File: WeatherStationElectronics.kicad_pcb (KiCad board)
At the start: 2 copper layers, 99.5 x 86 mm, 8 parts, among them J1 Barrel_Jack, SW1 SW_SPST, U1 ESP32-C3-DevKitM-1, U3 DHT11, U4 BMP280

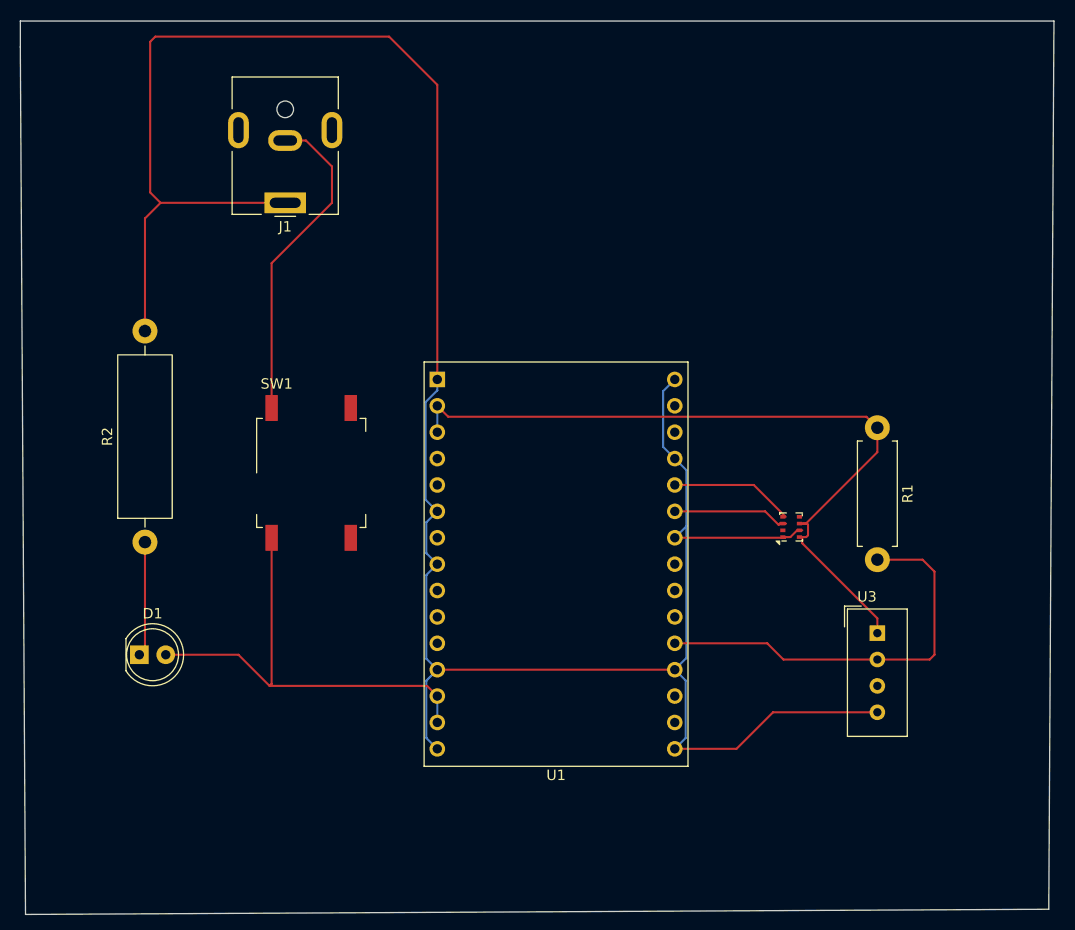
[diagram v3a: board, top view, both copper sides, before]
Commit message: Add mounting holes to the PCB
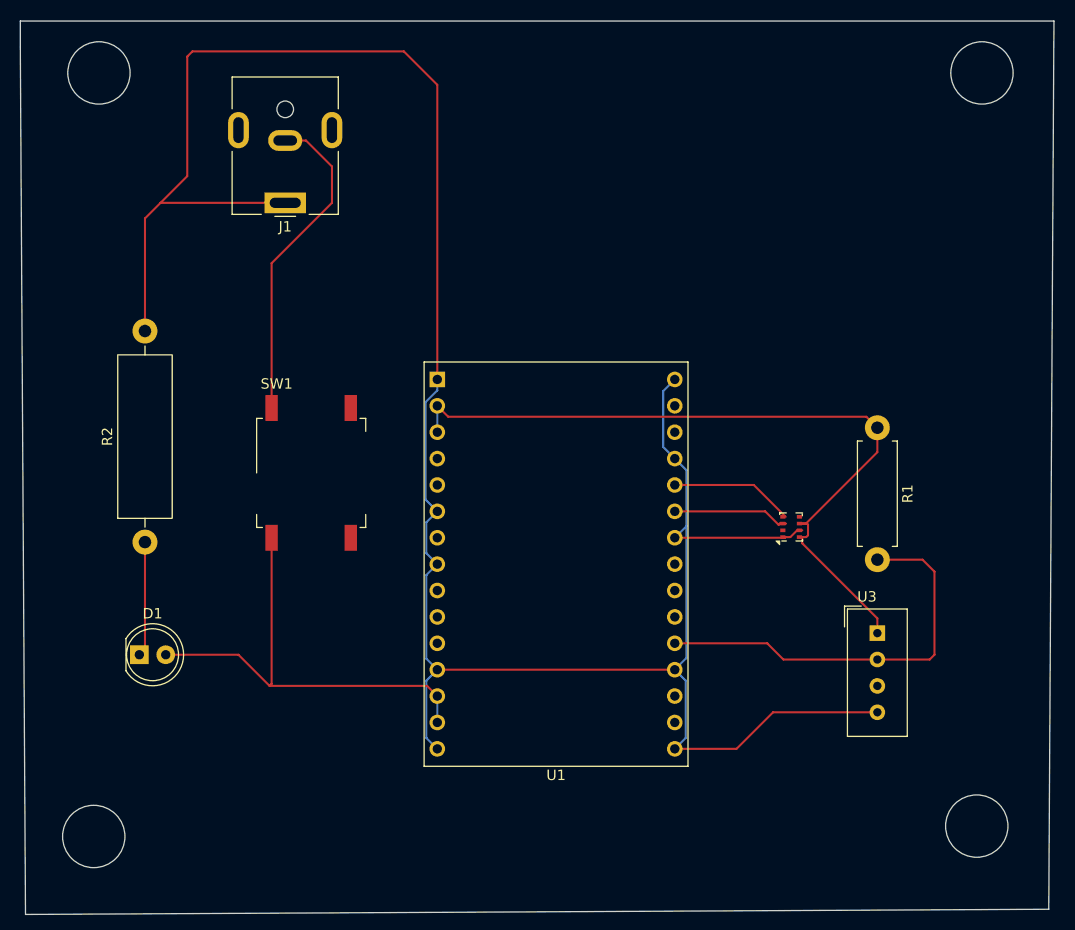
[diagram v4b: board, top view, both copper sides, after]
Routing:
- net GND: track 235.5 -> 230.6 mm
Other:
- outline, holes or cut-outs redrawn
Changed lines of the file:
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@@
 			)
 		)
-		(property "Datasheet" ""
+		(property "Datasheet" "~"
 			(at 0 0 0)
 			(layer "F.Fab")
@@
 			)
 		)
-		(property "Datasheet" ""
+		(property "Datasheet" "~"
 			(at 0 0 0)
 			(unlocked yes)
@@
 			)
 		)
-		(property "Datasheet" ""
+		(property "Datasheet" "~"
 			(at 0 0 90)
 			(layer "F.Fab")
@@
 		)
 		(property "Value" "Barrel_Jack"
-			(at -0.5 14.5 0)
+			(at -0.07 13.505 0)
 			(layer "F.Fab")
 			(effects
@@
 			)
 		)
-		(property "Datasheet" ""
+		(property "Datasheet" "~"
 			(at 0 0 180)
 			(unlocked yes)
@@
 			)
 		)
-		(property "Datasheet" ""
+		(property "Datasheet" "~"
 			(at 0 0 90)
 			(layer "F.Fab")
@@
 		(layer "Edge.Cuts")
 	)
+	(gr_circle
+		(center 48 54)
+		(end 51 54)
+		(stroke
+			(width 0.05)
+			(type solid)
+		)
+		(fill no)
+		(layer "Edge.Cuts")
+	)
 	(gr_line
 		(start 139.93 49.005)
@@
 		(layer "Edge.Cuts")
 	)
+	(gr_circle
+		(center 47.5 127.5)
+		(end 50.5 127.5)
+		(stroke
+			(width 0.05)
+			(type solid)
+		)
+		(fill no)
+		(layer "Edge.Cuts")
+	)
 	(gr_line
 		(start 40.93 135.005)
@@
 		(layer "Edge.Cuts")
 	)
+	(gr_circle
+		(center 132.5 126.5)
+		(end 135.5 126.5)
+		(stroke
+			(width 0.05)
+			(type solid)
+		)
+		(fill no)
+		(layer "Edge.Cuts")
+	)
+	(gr_circle
+		(center 133 54)
+		(end 136 54)
+		(stroke
+			(width 0.05)
+			(type solid)
+		)
+		(fill no)
+		(layer "Edge.Cuts")
+	)
 	(gr_line
 		(start 40.43 49.005)
@@
 	)
 	(segment
+		(start 56.5 52.425)
+		(end 56.5 63.935)
+		(width 0.2)
+		(layer "F.Cu")
+		(net 3)
+	)
+	(segment
 		(start 115.205 98.03)
 		(end 115.705 98.03)
@@
 	)
 	(segment
-		(start 53.43 50.505)
-		(end 52.93 51.005)
-		(width 0.2)
-		(layer "F.Cu")
-		(net 3)
-	)
-	(segment
-		(start 75.93 50.505)
-		(end 53.43 50.505)
-		(width 0.2)
-		(layer "F.Cu")
-		(net 3)
-	)
-	(segment
-		(start 80.57 55.145)
-		(end 75.93 50.505)
-		(width 0.2)
-		(layer "F.Cu")
-		(net 3)
-	)
-	(segment
 		(start 114.105 98.68)
 		(end 114.555 98.68)
@@
 	)
 	(segment
+		(start 77.35 51.925)
+		(end 57 51.925)
+		(width 0.2)
+		(layer "F.Cu")
+		(net 3)
+	)
+	(segment
 		(start 66.93 66.505)
 		(end 65.93 66.505)
@@
 	)
 	(segment
+		(start 80.57 55.145)
+		(end 77.35 51.925)
+		(width 0.2)
+		(layer "F.Cu")
+		(net 3)
+	)
+	(segment
+		(start 109.37 119.065)
+		(end 103.43 119.065)
+		(width 0.2)
+		(layer "F.Cu")
+		(net 3)
+	)
+	(segment
+		(start 52.43 68.005)
+		(end 53.93 66.505)
+		(width 0.2)
+		(layer "F.Cu")
+		(net 3)
+	)
+	(segment
+		(start 57 51.925)
+		(end 56.5 52.425)
+		(width 0.2)
+		(layer "F.Cu")
+		(net 3)
+	)
+	(segment
+		(start 122.93 115.545)
+		(end 112.89 115.545)
+		(width 0.2)
+		(layer "F.Cu")
+		(net 3)
+	)
+	(segment
 		(start 80.57 83.505)
 		(end 80.57 55.145)
@@
 	)
 	(segment
-		(start 109.37 119.065)
-		(end 103.43 119.065)
-		(width 0.2)
-		(layer "F.Cu")
-		(net 3)
-	)
-	(segment
-		(start 52.43 68.005)
-		(end 53.93 66.505)
-		(width 0.2)
-		(layer "F.Cu")
-		(net 3)
-	)
-	(segment
-		(start 122.93 115.545)
-		(end 112.89 115.545)
-		(width 0.2)
-		(layer "F.Cu")
-		(net 3)
-	)
-	(segment
 		(start 80.57 111.445)
 		(end 103.43 111.445)
@@
 	)
 	(segment
-		(start 52.93 51.005)
-		(end 52.93 65.505)
+		(start 56.5 63.935)
+		(end 53.93 66.505)
 		(width 0.2)
 		(layer "F.Cu")
@@
 		(width 0.2)
 		(layer "F.Cu")
-		(net 3)
-	)
-	(segment
-		(start 52.93 65.505)
-		(end 53.93 66.505)
-		(width 0.2)
-		(layer "F.Cu")

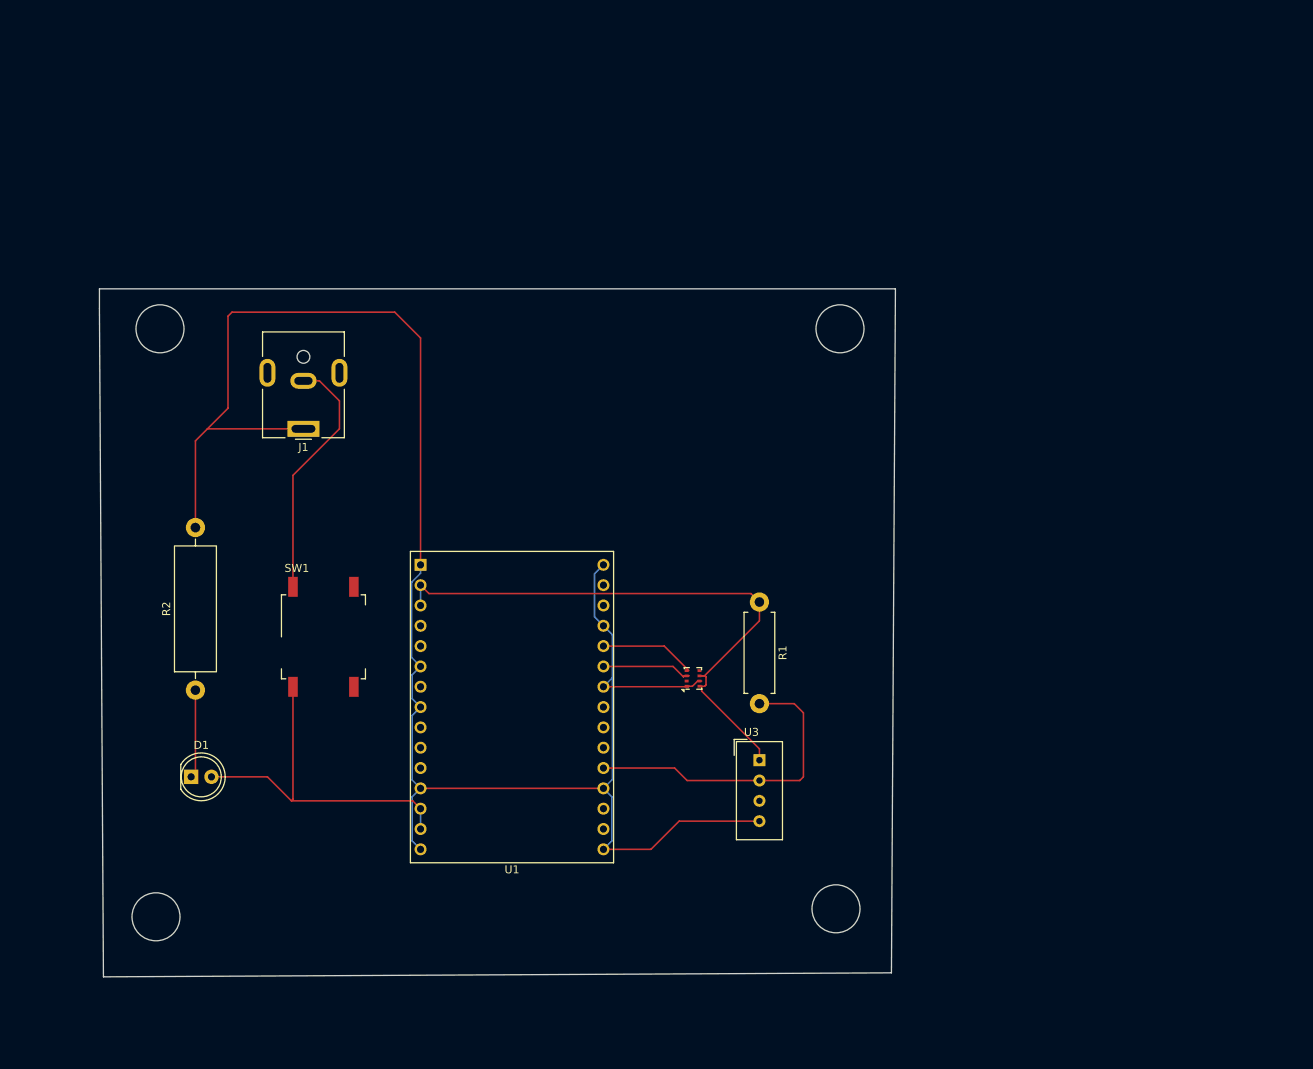
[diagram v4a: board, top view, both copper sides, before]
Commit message: update PCB
Make mounting holes and fill all the board area with copper connected to
the ground
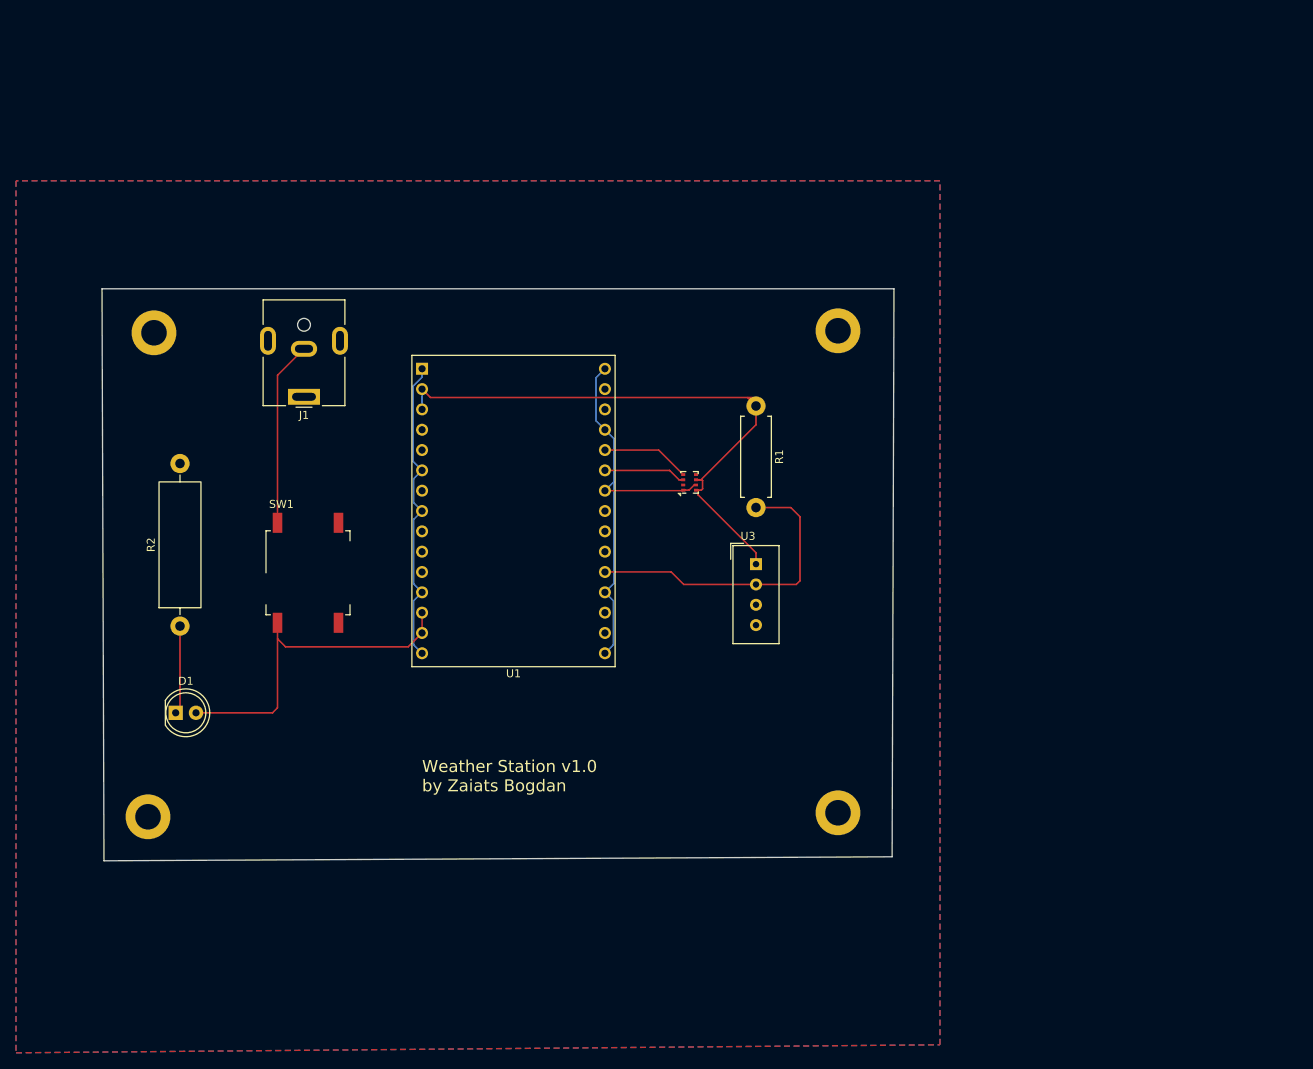
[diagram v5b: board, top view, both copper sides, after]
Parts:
- added M3: MountingHole_3.2mm_M3_DIN965_Pad, MountingHole:MountingHole_3.2mm_M3_DIN965_Pad, F.Cu at (132.8, 54.2)
- added REF**: MountingHole_3.2mm_M3_DIN965_Pad, MountingHole:MountingHole_3.2mm_M3_DIN965_Pad, F.Cu at (46.5, 115.0)
- added REF**: MountingHole_3.2mm_M3_DIN965_Pad, MountingHole:MountingHole_3.2mm_M3_DIN965_Pad, F.Cu at (47.2, 54.5)
- added REF**: MountingHole_3.2mm_M3_DIN965_Pad, MountingHole:MountingHole_3.2mm_M3_DIN965_Pad, F.Cu at (132.8, 114.5)
- moved R1 24.5 mm to (122.5, 63.6)
- moved U3 24.5 mm to (122.5, 83.4)
- moved U4 24.5 mm to (114.2, 73.2)
- moved U1 24.5 mm to (80.8, 59.0)
- moved R2 8.23 mm to (50.5, 91.2)
- moved SW1 8.23 mm to (66.5, 84.5)
- moved D1 8.23 mm to (50.0, 102.0)
- moved J1 4.01 mm to (66.0, 62.5)
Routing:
- net GND: track 230.6 -> 91.6 mm
- net Net-(SW1-A): track 31.2 -> 23.1 mm
- net +5V: track 44.7 -> 42.8 mm
- net Net-(U1-IO9): track 11.9 -> 11.1 mm
- net Net-(U1-IO4): track 39.8 -> 39.2 mm
- net Net-(U1-IO8): track 11.8 -> 11.3 mm
- added copper zone on B.Cu, net GND
- added copper zone on F.Cu, net GND
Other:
- board size 99.5 x 86 mm -> 99 x 71.5 mm
- board text added: "Weather Station v1.0 by Zaiats Bogdan"
